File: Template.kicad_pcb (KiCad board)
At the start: 2 copper layers, 70 x 70 mm, 5 parts, among them J1 Conn_02x10_Odd_Even, J2 Conn_01x08, J3 Conn_01x08

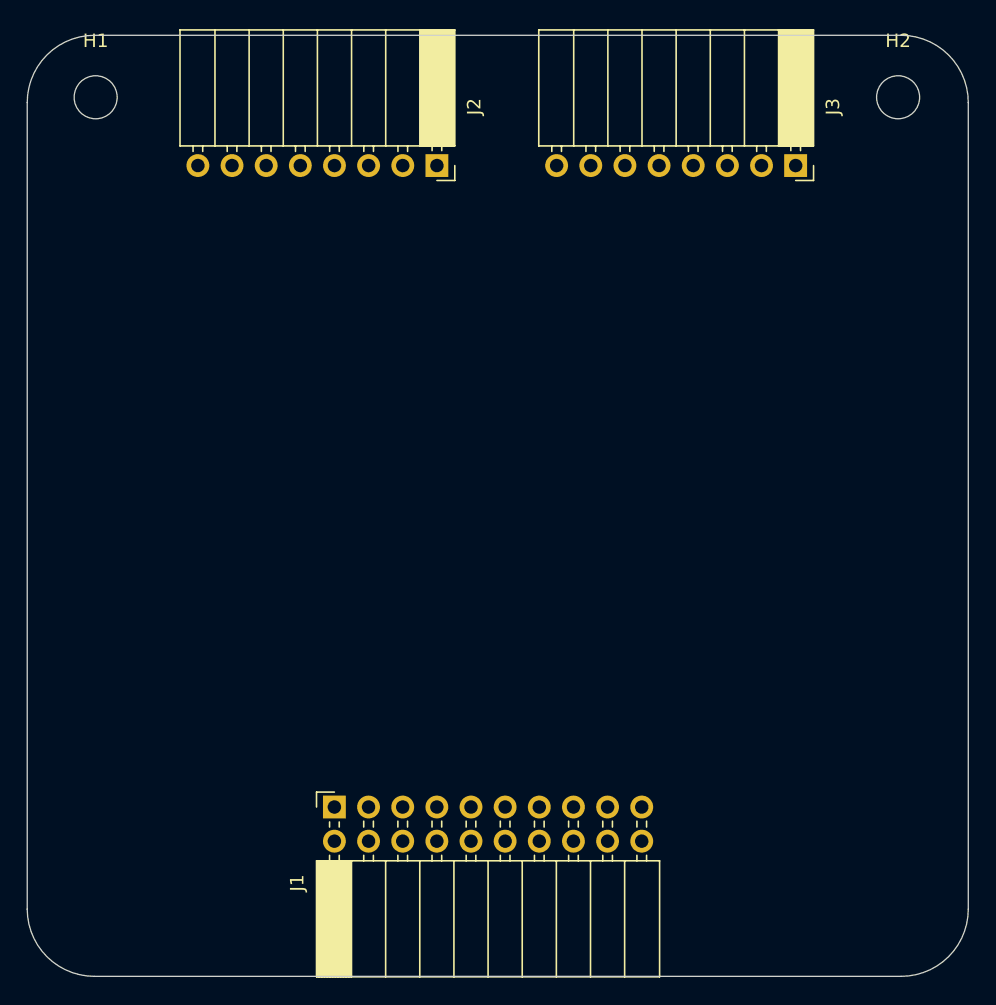
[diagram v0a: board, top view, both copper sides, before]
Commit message: Placed things in metrics not with rnd()
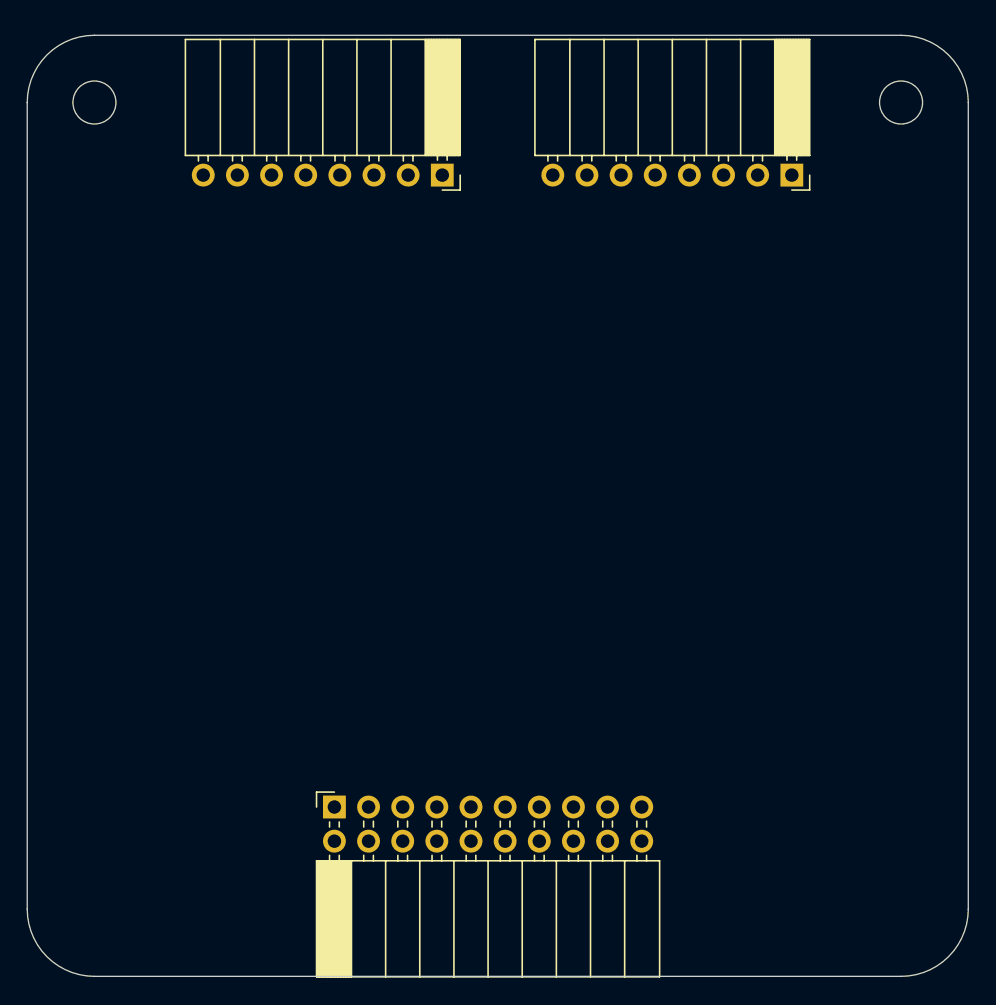
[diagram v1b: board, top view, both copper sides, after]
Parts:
- moved J2 0.81 mm to (110.9, 60.4)
- moved J3 0.77 mm to (136.9, 60.4)
- moved H2 0.45 mm to (145.0, 55.0)
- moved H1 0.40 mm to (85.0, 55.0)
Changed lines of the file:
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@@
   (net 27 "unconnected-(J3-Pad2)")
   (footprint "Connector_PinSocket_2.54mm:PinSocket_1x08_P2.54mm_Horizontal" (layer "F.Cu")
-    (at 137.16 59.69 -90)
+    (at 136.875 60.4 -90)
     (descr "Through hole angled socket strip, 1x08, 2.54mm pitch, 8.51mm socket length, single row (from Kicad 4.0.7), script generated")
     (tags "Through hole angled socket strip THT 1x08 2.54mm single row")
@@
     (property "Sheetname" "IO")
     (attr through_hole)
-    (fp_text reference "J3" (at -4.38 -2.77 90) (layer "F.SilkS")
-      (effects (font (size 1 1) (thickness 0.15)))
-    )
-    (fp_text value "Conn_01x08" (at -4.38 20.55 90) (layer "F.Fab")
-      (effects (font (size 1 1) (thickness 0.15)))
-    )
-    (fp_text user "${REFERENCE}" (at -5.775 8.89) (layer "F.Fab")
+    (fp_text reference "J3" (at -4.38 -2.77 90) (layer "F.SilkS") hide
+      (effects (font (size 1 1) (thickness 0.15)))
+    )
+    (fp_text value "Conn_01x08" (at -4.38 20.55 90) (layer "F.Fab") hide
+      (effects (font (size 1 1) (thickness 0.15)))
+    )
+    (fp_text user "${REFERENCE}" (at -5.775 8.89) (layer "F.Fab") hide
       (effects (font (size 1 1) (thickness 0.15)))
     )
@@
   )
   (footprint "MountingHole:MountingHole_3.2mm_M3" (layer "F.Cu")
-    (at 85.09 54.61)
+    (at 85 55)
     (descr "Mounting Hole 3.2mm, no annular, M3")
     (tags "mounting hole 3.2mm no annular m3")
@@
     (property "Sheetname" "IO")
     (attr exclude_from_pos_files)
-    (fp_text reference "H1" (at 0 -4.2) (layer "F.SilkS")
-      (effects (font (size 1 1) (thickness 0.15)))
-    )
-    (fp_text value "MountingHole" (at 0 4.2) (layer "F.Fab")
-      (effects (font (size 1 1) (thickness 0.15)))
-    )
-    (fp_text user "${REFERENCE}" (at 0 0) (layer "F.Fab")
+    (fp_text reference "H1" (at 0 -4.2) (layer "F.SilkS") hide
+      (effects (font (size 1 1) (thickness 0.15)))
+    )
+    (fp_text value "MountingHole" (at 0 4.2) (layer "F.Fab") hide
+      (effects (font (size 1 1) (thickness 0.15)))
+    )
+    (fp_text user "${REFERENCE}" (at 0 0) (layer "F.Fab") hide
       (effects (font (size 1 1) (thickness 0.15)))
     )
@@
   )
   (footprint "Connector_PinSocket_2.54mm:PinSocket_1x08_P2.54mm_Horizontal" (layer "F.Cu")
-    (at 110.475 59.69 -90)
+    (at 110.875 60.4 -90)
     (descr "Through hole angled socket strip, 1x08, 2.54mm pitch, 8.51mm socket length, single row (from Kicad 4.0.7), script generated")
     (tags "Through hole angled socket strip THT 1x08 2.54mm single row")
@@
     (property "Sheetname" "IO")
     (attr through_hole)
-    (fp_text reference "J2" (at -4.38 -2.77 90) (layer "F.SilkS")
-      (effects (font (size 1 1) (thickness 0.15)))
-    )
-    (fp_text value "Conn_01x08" (at -4.38 20.55 90) (layer "F.Fab")
-      (effects (font (size 1 1) (thickness 0.15)))
-    )
-    (fp_text user "${REFERENCE}" (at -5.775 8.89) (layer "F.Fab")
+    (fp_text reference "J2" (at -4.38 -2.77 90) (layer "F.SilkS") hide
+      (effects (font (size 1 1) (thickness 0.15)))
+    )
+    (fp_text value "Conn_01x08" (at -4.38 20.55 90) (layer "F.Fab") hide
+      (effects (font (size 1 1) (thickness 0.15)))
+    )
+    (fp_text user "${REFERENCE}" (at -5.775 8.89) (layer "F.Fab") hide
       (effects (font (size 1 1) (thickness 0.15)))
     )
@@
     (property "Sheetname" "IO")
     (attr through_hole)
-    (fp_text reference "J1" (at -5.65 -2.77 90) (layer "F.SilkS")
-      (effects (font (size 1 1) (thickness 0.15)))
-    )
-    (fp_text value "Conn_02x10_Odd_Even" (at -5.65 25.63 90) (layer "F.Fab")
-      (effects (font (size 1 1) (thickness 0.15)))
-    )
-    (fp_text user "${REFERENCE}" (at -8.315 11.43) (layer "F.Fab")
+    (fp_text reference "J1" (at -5.65 -2.77 90) (layer "F.SilkS") hide
+      (effects (font (size 1 1) (thickness 0.15)))
+    )
+    (fp_text value "Conn_02x10_Odd_Even" (at -5.65 25.63 90) (layer "F.Fab") hide
+      (effects (font (size 1 1) (thickness 0.15)))
+    )
+    (fp_text user "${REFERENCE}" (at -8.315 11.43) (layer "F.Fab") hide
       (effects (font (size 1 1) (thickness 0.15)))
     )
@@
   )
   (footprint "MountingHole:MountingHole_3.2mm_M3" (layer "F.Cu")
-    (at 144.78 54.61)
+    (at 145 55)
     (descr "Mounting Hole 3.2mm, no annular, M3")
     (tags "mounting hole 3.2mm no annular m3")
@@
     (property "Sheetname" "IO")
     (attr exclude_from_pos_files)
-    (fp_text reference "H2" (at 0 -4.2) (layer "F.SilkS")
-      (effects (font (size 1 1) (thickness 0.15)))
-    )
-    (fp_text value "MountingHole" (at 0 4.2) (layer "F.Fab")
-      (effects (font (size 1 1) (thickness 0.15)))
-    )
-    (fp_text user "${REFERENCE}" (at 0 0) (layer "F.Fab")
-      (effects (font (size 1 1) (thickness 0.15)))
-    )
+    (fp_text reference "H2" (at 0 -4.2) (layer "F.SilkS") hide
+      (effects (font (size 1 1) (thickness 0.15)))
+    )
+    (fp_text value "MountingHole" (at 0 4.2) (layer "F.Fab") hide
+      (effects (font (size 1 1) (thickness 0.15)))
+    )
+    (fp_text user "${REFERENCE}" (at 0 0) (layer "F.Fab") hide
+      (effects (font (size 1 1) (thickness 0.15)))
+    )

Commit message: Small edit
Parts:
- moved J1 0.70 mm to (103.5, 107.4)
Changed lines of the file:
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@@
   )
   (footprint "Connector_PinSocket_2.54mm:PinSocket_2x10_P2.54mm_Horizontal" (layer "F.Cu")
-    (at 102.85 107.405 90)
+    (at 103.55 107.375 90)
     (descr "Through hole angled socket strip, 2x10, 2.54mm pitch, 8.51mm socket length, double cols (from Kicad 4.0.7), script generated")
     (tags "Through hole angled socket strip THT 2x10 2.54mm double row")

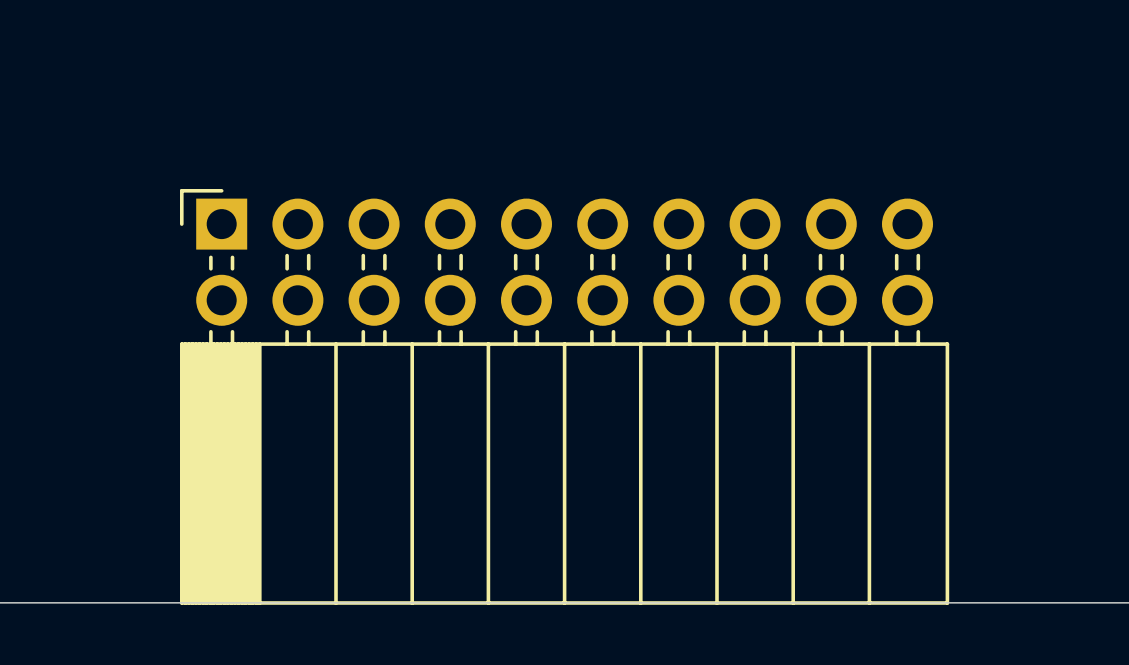
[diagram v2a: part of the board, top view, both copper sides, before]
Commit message: CONNECTOR
Main connector position adjustment.
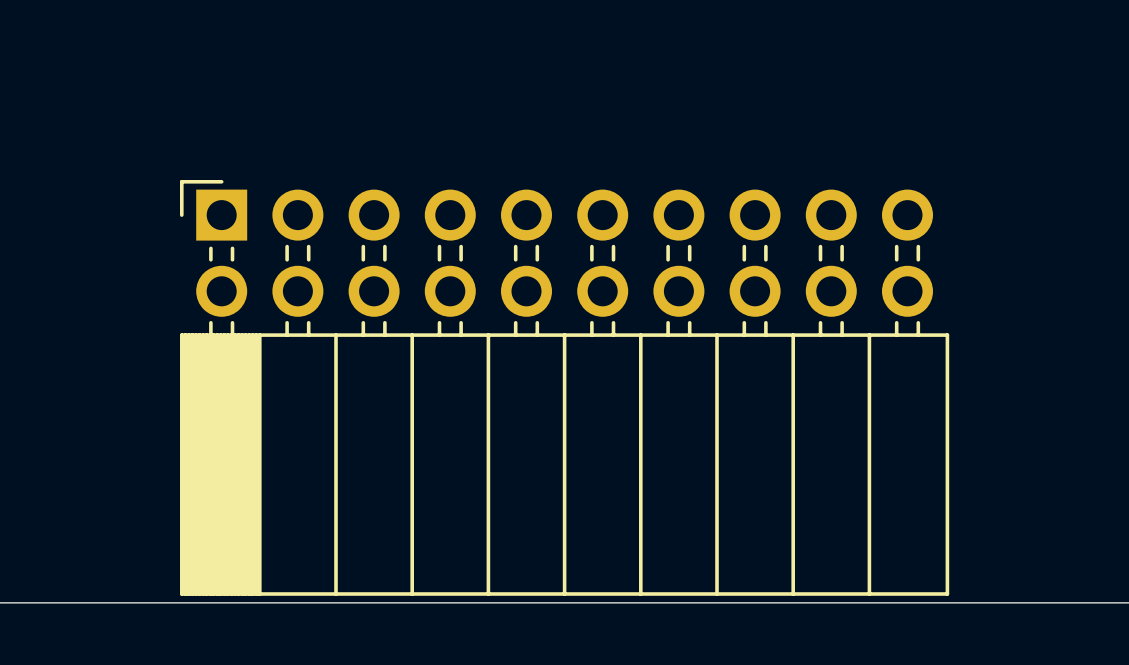
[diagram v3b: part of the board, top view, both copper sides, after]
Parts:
- moved J1 0.30 mm to (103.5, 107.1)
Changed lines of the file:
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@@
   )
   (footprint "Connector_PinSocket_2.54mm:PinSocket_2x10_P2.54mm_Horizontal" (layer "F.Cu")
-    (at 103.55 107.375 90)
+    (at 103.55 107.075 90)
     (descr "Through hole angled socket strip, 2x10, 2.54mm pitch, 8.51mm socket length, double cols (from Kicad 4.0.7), script generated")
     (tags "Through hole angled socket strip THT 2x10 2.54mm double row")
@@
   (gr_arc (start 85 120) (mid 81.464466 118.535534) (end 80 115) (layer "Edge.Cuts") (width 0.05))
   (gr_arc (start 150 115) (mid 148.535534 118.535534) (end 145 120) (layer "Edge.Cuts") (width 0.05))
-  (gr_text "Physical connector" (at 115 116) (layer "Dwgs.User")
+  (gr_text "Physical connector" (at 114.9604 115.9256) (layer "Dwgs.User")
     (effects (font (size 1 1) (thickness 0.15)))
   )
-  (segment (start 115.555 107.4) (end 115.55 107.405) (width 0.25) (layer "F.Cu") (net 13))
 )
